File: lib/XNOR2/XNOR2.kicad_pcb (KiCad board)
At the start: 2 copper layers, 10 parts, among them P1 PMOS, P2 PMOS, P3 PMOS, P4 PMOS, P5 PMOS

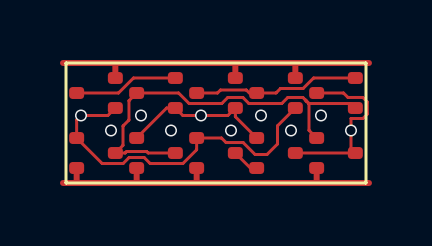
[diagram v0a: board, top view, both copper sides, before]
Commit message: Layout of XOR2 and XNOR2, in both orientations. That nut was hard to crack !!
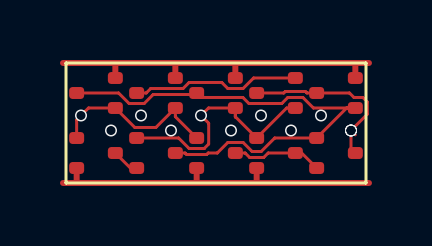
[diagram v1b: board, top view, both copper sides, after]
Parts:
- moved P3 4.00 mm to (3.00, 1.00)
- moved P2 2.00 mm to (5.00, 1.00)
- moved P4 2.00 mm to (7.00, 1.00)
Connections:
- N1 pad 3: inor -> sndNA
- N2 pad 2: GND -> sndNA
- N2 pad 3: inor -> inand
- N3 pad 3: sndNA -> nmid
- N4 pad 2: sndNA -> GND
- N4 pad 3: Y -> nmid
- N5 pad 1: inor -> inand
- N5 pad 2: GND -> nmid
- P1 pad 3: sndPA -> inand
- P2 pad 2: sndPA -> VDD
- P2 pad 3: inor -> inand
- P3 pad 3: pmid -> sndPA
- P4 pad 2: VDD -> sndPA
- P4 pad 3: pmid -> Y
- P5 pad 1: inor -> inand
- P5 pad 2: pmid -> VDD
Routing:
- net inand: track 0.00 -> 16.9 mm
- net inor: track 13.8 -> 0.00 mm
- net A: track 11.7 -> 5.89 mm
- net pmid: track 5.58 -> 0.00 mm
- net B: track 5.21 -> 8.53 mm
- net nmid: track 0.00 -> 3.04 mm
- net sndPA: track 3.50 -> 5.66 mm
- net VDD: track 11.7 -> 12.2 mm
- net GND: track 12.3 -> 11.7 mm
- net Y: track 6.03 -> 6.05 mm, vias 1 -> 2
